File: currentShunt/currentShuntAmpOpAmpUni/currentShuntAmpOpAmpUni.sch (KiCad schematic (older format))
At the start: 11 parts, among them Q1 2N3906, U1 AD822A

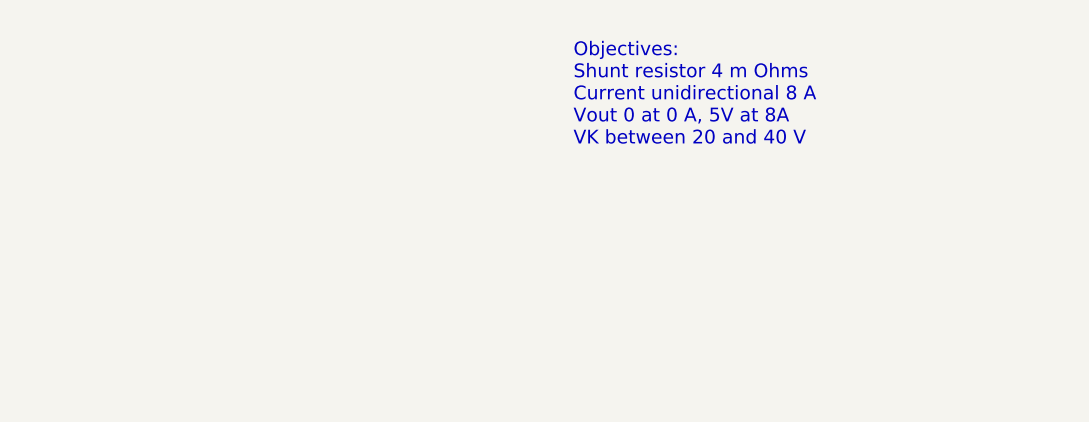
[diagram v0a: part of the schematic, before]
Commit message: update ref to spreadsheet
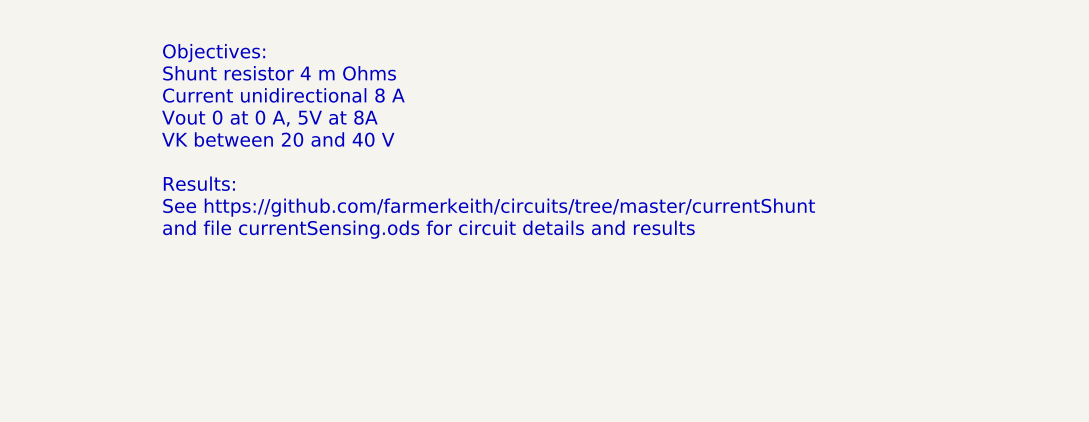
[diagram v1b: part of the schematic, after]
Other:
- note added: "Objectives:\nShunt resistor 4 m Ohms\nCurrent unidirectional 8 A\nVout 0 at 0 A, 5V at 8A\nVK between 20 and 40 V\n\nResults:\nSee https://github.com/farmerkeith/circuits/tree/master/currentShunt \nand file currentSensing.ods for circuit details and results"
- note removed: "Objectives:\nShunt resistor 4 m Ohms\nCurrent unidirectional 8 A\nVout 0 at 0 A, 5V at 8A\nVK between 20 and 40 V"
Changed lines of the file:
@@
 Wire Wire Line
 	1600 600  1600 800
-Text Notes 9600 1100 0    60   ~ 0
-Objectives:\nShunt resistor 4 m Ohms\nCurrent unidirectional 8 A\nVout 0 at 0 A, 5V at 8A\nVK between 20 and 40 V
+Text Notes 7800 1500 0    60   ~ 0
+Objectives:\nShunt resistor 4 m Ohms\nCurrent unidirectional 8 A\nVout 0 at 0 A, 5V at 8A\nVK between 20 and 40 V\n\nResults:\nSee https://github.com/farmerkeith/circuits/tree/master/currentShunt \nand file currentSensing.ods for circuit details and results
 Connection ~ 3800 3050
 Connection ~ 3800 700
